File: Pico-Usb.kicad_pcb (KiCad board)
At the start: 2 copper layers, 25 x 60 mm, 40 parts, among them J1 USB_A, J2 10133475-10001LF, J3 MEM2067-02-180-00-A_REVB, U1 MAX40200AUK, U2 MAX40200AUK, U3 W25Q128JVS, U4 AP2112K-3.3, U5 RP2040, U6 TS3USB221ARSER, Y1 ABM3B-12.000MHZ-10-1-U-T

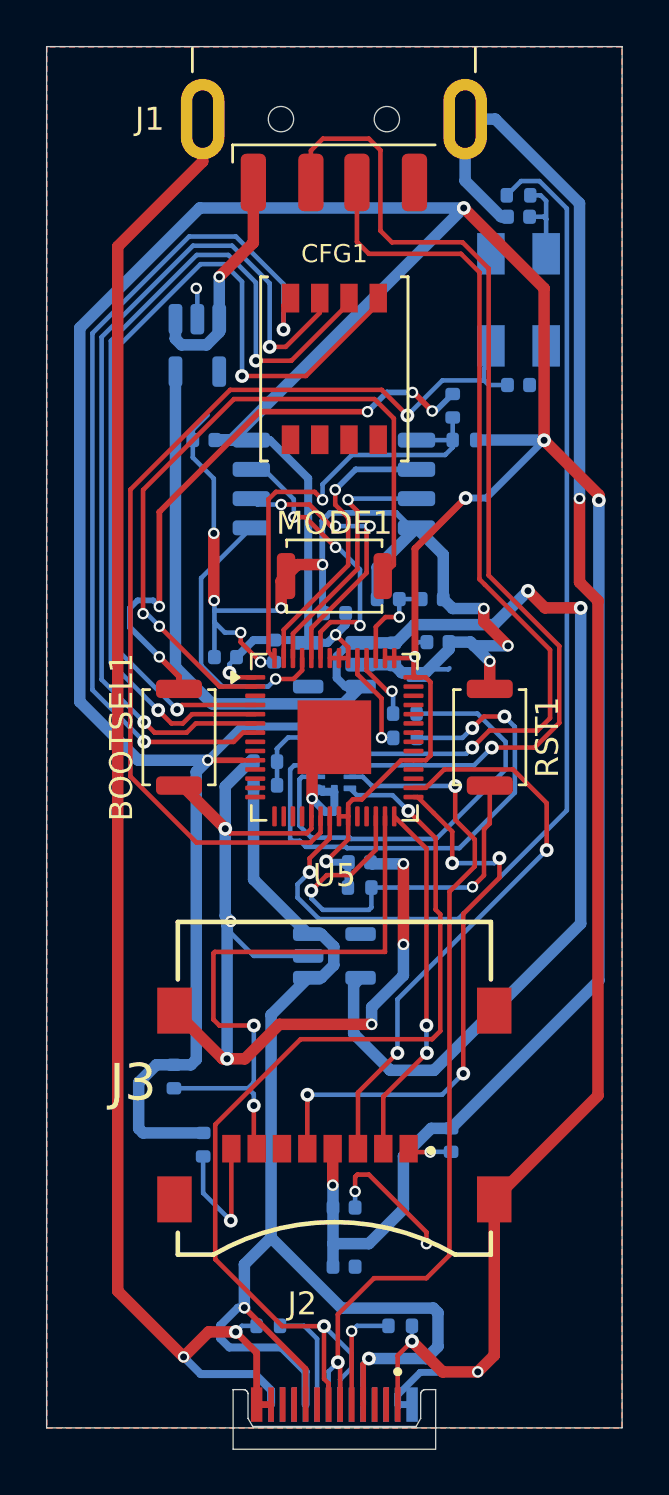
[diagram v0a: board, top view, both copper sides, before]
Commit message: Modifique los componentes originales por unos que si se encuentran
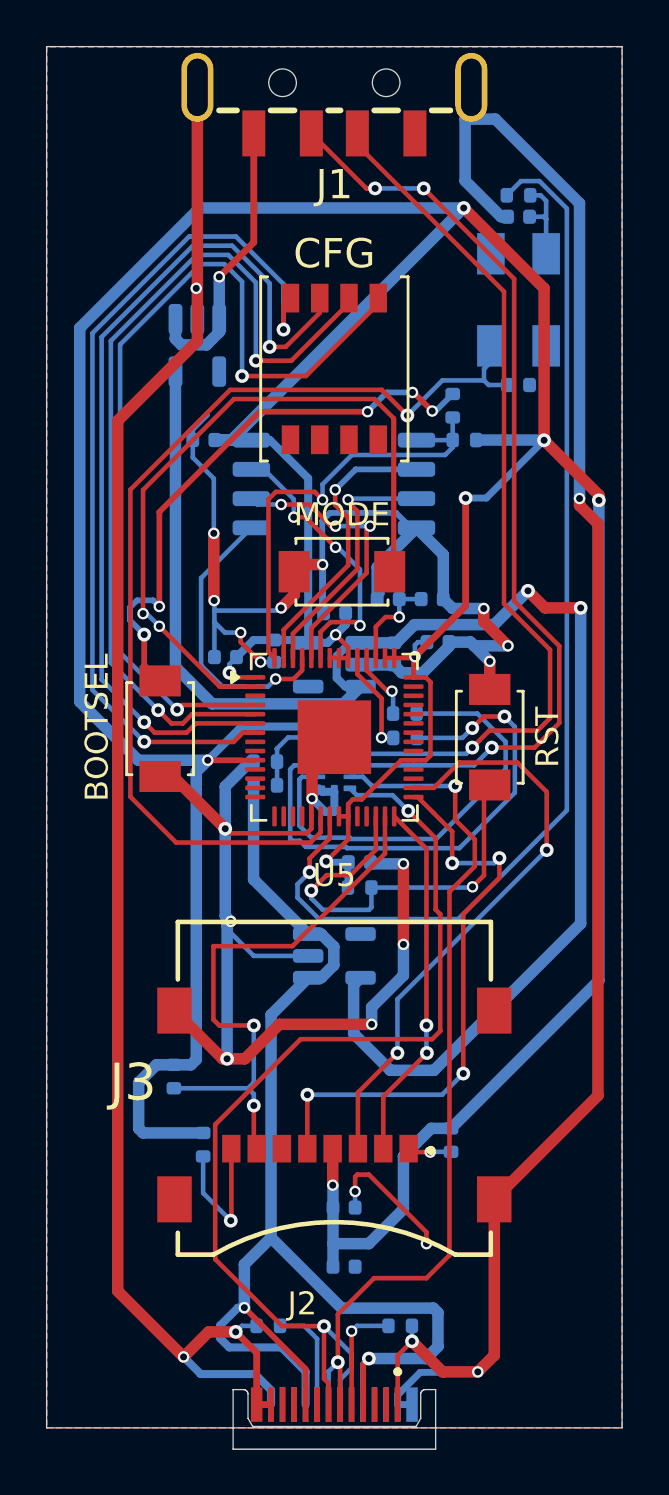
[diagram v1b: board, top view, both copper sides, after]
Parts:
- removed BOOTSEL1, MODE1, RST1: SW_Push, Button_Switch_SMD:SW_Push_SPST_NO_Alps_SKRK
- added BOOTSEL: TS-1088-AR02016, Custom_Switchs:SW_TS-1088-AR02016, F.Cu at (129.9, 99.6)
- added MODE: TS-1088-AR02016, Custom_Switchs:SW_TS-1088-AR02016, F.Cu at (137.8, 92.8)
- added RST: TS-1088-AR02016, Custom_Switchs:SW_TS-1088-AR02016, F.Cu at (144.2, 100.0)
- J1: value USB_A -> USB_AM_180-WT; footprint Connector_USB:USB_A_CNCTech_1001-011-01101_Horizontal -> Custom_Connectors:USB-AM-180-WT
- moved J1 6.52 mm to (137.5, 72.8), turned to 180 degrees
- renumbered CFG1 to CFG
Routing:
- net Net-(U5-GPIO0): track 31.5 -> 38.2 mm
- net /USB_A_D-: track 44.6 -> 41.4 mm, vias 1 -> 3
- net /SPI_RX: track 26.9 -> 24.6 mm
- net Net-(U1-EN): track 10.2 -> 12.4 mm
- net GNDREF: track 261.6 -> 259.9 mm
- net Net-(BOOTSEL1-Pad1): track 25.6 -> 24.9 mm
- net /SPI_TX: track 25.1 -> 25.7 mm
- net Net-(U5-XIN): track 43.8 -> 44.3 mm

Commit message: Verifique una vez más conexiones
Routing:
- net GNDREF: track 259.9 -> 259.3 mm
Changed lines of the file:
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@@
 			)
 		)
+		(model "${KIPRJMOD}/kicad_libs/Custom_ICs.pretty/TS3USB221ARSER.step"
+			(offset
+				(xyz 0 0 0)
+			)
+			(scale
+				(xyz 1 1 1)
+			)
+			(rotate
+				(xyz -90 -0 -0)
+			)
+		)
 	)
 	(footprint "Resistor_SMD:R_0402_1005Metric"
@@
 	)
 	(segment
-		(start 134.125 126.743058)
-		(end 133.215 125.833058)
-		(width 0.3)
-		(layer "F.Cu")
-		(net "GNDREF")
-	)
-	(segment
 		(start 132.263109 91.143678)
 		(end 132.263109 94.046023)
@@
 	)
 	(segment
+		(start 134.75 127.368058)
+		(end 133.215 125.833058)
+		(width 0.2)
+		(layer "F.Cu")
+		(net "GNDREF")
+	)
+	(segment
 		(start 143.73 127.57)
 		(end 142.202316 127.57)
@@
 	)
 	(segment
+		(start 134.75 128.99)
+		(end 134.75 127.368058)
+		(width 0.2)
+		(layer "F.Cu")
+		(net "GNDREF")
+	)
+	(segment
 		(start 138.401781 119.731537)
 		(end 138.401781 119.098219)
@@
 	)
 	(segment
-		(start 134.125 128.99)
-		(end 134.125 126.743058)
-		(width 0.3)
-		(layer "F.Cu")
-		(net "GNDREF")
-	)
-	(segment
 		(start 132.036942 125.833058)
 		(end 130.95 126.92)
@@
 	)
 	(segment
-		(start 134.75 128.99)
-		(end 134.125 128.99)
-		(width 0.3)
-		(layer "F.Cu")
-		(net "GNDREF")
-	)
-	(segment
 		(start 148.95 115.57)
 		(end 148.95 90.730661)
@@
 	)
 	(segment
-		(start 134.75 128.99)
-		(end 134.75 128.365)
-		(width 0.35)
-		(layer "B.Cu")
-		(net "GNDREF")
-	)
-	(segment
 		(start 137.313148 90.255477)
 		(end 140.181545 90.255477)
@@
 	)
 	(segment
-		(start 140.25 128.572918)
-		(end 141.231828 127.59109)
-		(width 0.3)
-		(layer "B.Cu")
-		(net "GNDREF")
-	)
-	(segment
 		(start 136.95 92.4625)
 		(end 136.9875 92.5)
@@
 	)
 	(segment
-		(start 134.05 127.665)
-		(end 131.695 127.665)
+		(start 134.75 128.365)
+		(end 133.465 127.08)
 		(width 0.35)
 		(layer "B.Cu")
@@
 	)
 	(segment
+		(start 140.25 128.99)
+		(end 140.25 127.98)
+		(width 0.2)
+		(layer "B.Cu")
+		(net "GNDREF")
+	)
+	(segment
+		(start 140.66 127.57)
+		(end 143.73 127.57)
+		(width 0.2)
+		(layer "B.Cu")
+		(net "GNDREF")
+	)
+	(segment
 		(start 131.5475 80.5475)
 		(end 131.5 80.5)
@@
 	)
 	(segment
+		(start 131.11 127.08)
+		(end 130.95 126.92)
+		(width 0.35)
+		(layer "B.Cu")
+		(net "GNDREF")
+	)
+	(segment
 		(start 134.299681 96.74)
 		(end 134.291934 96.732253)
@@
 	)
 	(segment
+		(start 134.75 128.99)
+		(end 134.75 128.365)
+		(width 0.35)
+		(layer "B.Cu")
+		(net "GNDREF")
+	)
+	(segment
 		(start 142.64 94.41)
 		(end 142.23 94)
@@
 	)
 	(segment
-		(start 131.695 127.665)
-		(end 130.95 126.92)
-		(width 0.35)
+		(start 140.25 127.98)
+		(end 140.66 127.57)
+		(width 0.2)
 		(layer "B.Cu")
 		(net "GNDREF")
@@
 	)
 	(segment
-		(start 140.25 128.99)
-		(end 140.875 128.99)
-		(width 0.3)
-		(layer "B.Cu")
-		(net "GNDREF")
-	)
-	(segment
 		(start 138.400712 119.732606)
 		(end 138.401781 119.731537)
@@
 	)
 	(segment
-		(start 141.231828 127.59109)
-		(end 143.70891 127.59109)
-		(width 0.3)
-		(layer "B.Cu")
-		(net "GNDREF")
-	)
-	(segment
 		(start 133.84 101.06)
 		(end 133.99 101.06)
@@
 	)
 	(segment
-		(start 134.75 128.365)
-		(end 134.05 127.665)
-		(width 0.35)
-		(layer "B.Cu")
-		(net "GNDREF")
-	)
-	(segment
 		(start 142.23 94)
 		(end 142.23 92.0675)
@@
 	)
 	(segment
+		(start 133.465 127.08)
+		(end 131.11 127.08)
+		(width 0.35)
+		(layer "B.Cu")
+		(net "GNDREF")
+	)
+	(segment
 		(start 137.105147 103.24)
 		(end 136.529999 102.664852)
@@
 		(layer "B.Cu")
 		(net "GNDREF")
-	)
-	(segment
-		(start 140.25 128.99)
-		(end 140.25 128.572918)
-		(width 0.3)
-		(layer "B.Cu")
-		(net "GNDREF")
